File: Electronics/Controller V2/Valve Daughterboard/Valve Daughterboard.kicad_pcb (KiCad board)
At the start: 2 copper layers, 62 x 69.5 mm, 25 parts, among them J1 Conn_01x08, J10 Conn_01x10, J11 Conn_01x02, J12 Conn_01x02, J13 Conn_01x02, J14 Conn_01x02, J15 Conn_01x02, J16 Conn_01x02, J17 Conn_01x02, J18 Conn_01x02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

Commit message: Completed daughterboards.
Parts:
- H1, H2, H3, H4: footprint MountingHole:MountingHole_3.2mm_M3 -> MountingHole:MountingHole_6.4mm_M6
- moved J10 24.0 mm to (98.7, 92.1), turned to -90 degrees
- moved J20 23.3 mm to (91.5, 92.1), turned to -90 degrees
- moved J1 14.7 mm to (146.4, 70.2), turned to -90 degrees
- moved J19 13.8 mm to (140.6, 70.2), turned to -90 degrees
- moved H3 4.24 mm to (88.5, 124.5)
- moved H4 3.91 mm to (143.0, 124.5)
- moved H1 3.00 mm to (88.5, 60.0)
- moved H2 2.50 mm to (143.0, 60.0)
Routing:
- net /VALVE_E_MB: track 0.00 -> 129.7 mm
- net /VALVE_E_MA: track 0.00 -> 115.4 mm
- net /VALVE_D_MB: track 0.00 -> 101.2 mm
- net /VALVE_D_MA: track 0.00 -> 87.0 mm
- net /VALVE_C_MB: track 0.00 -> 72.8 mm
- net Net-(J11-Pin_1): track 0.00 -> 68.4 mm
- net +12V: track 0.00 -> 66.3 mm
- net Net-(J12-Pin_1): track 0.00 -> 61.8 mm
- net /VALVE_C_MA: track 0.00 -> 58.5 mm
- net /VALVE_B_DIR: track 0.00 -> 54.2 mm
- net Net-(J3-Pin_2): track 0.00 -> 49.7 mm
- net /VALVE_B_PWM: track 0.00 -> 48.1 mm
- net Net-(J2-Pin_2): track 0.00 -> 47.9 mm
- net /VALVE_B_MB: track 0.00 -> 45.5 mm
- net /VALVE_C_DIR: track 0.00 -> 42.1 mm
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- added copper zone on B.Cu, net GND
- added copper zone on F.Cu, net GND
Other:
- board size 62 x 69.5 mm -> 68.5 x 78.5 mm

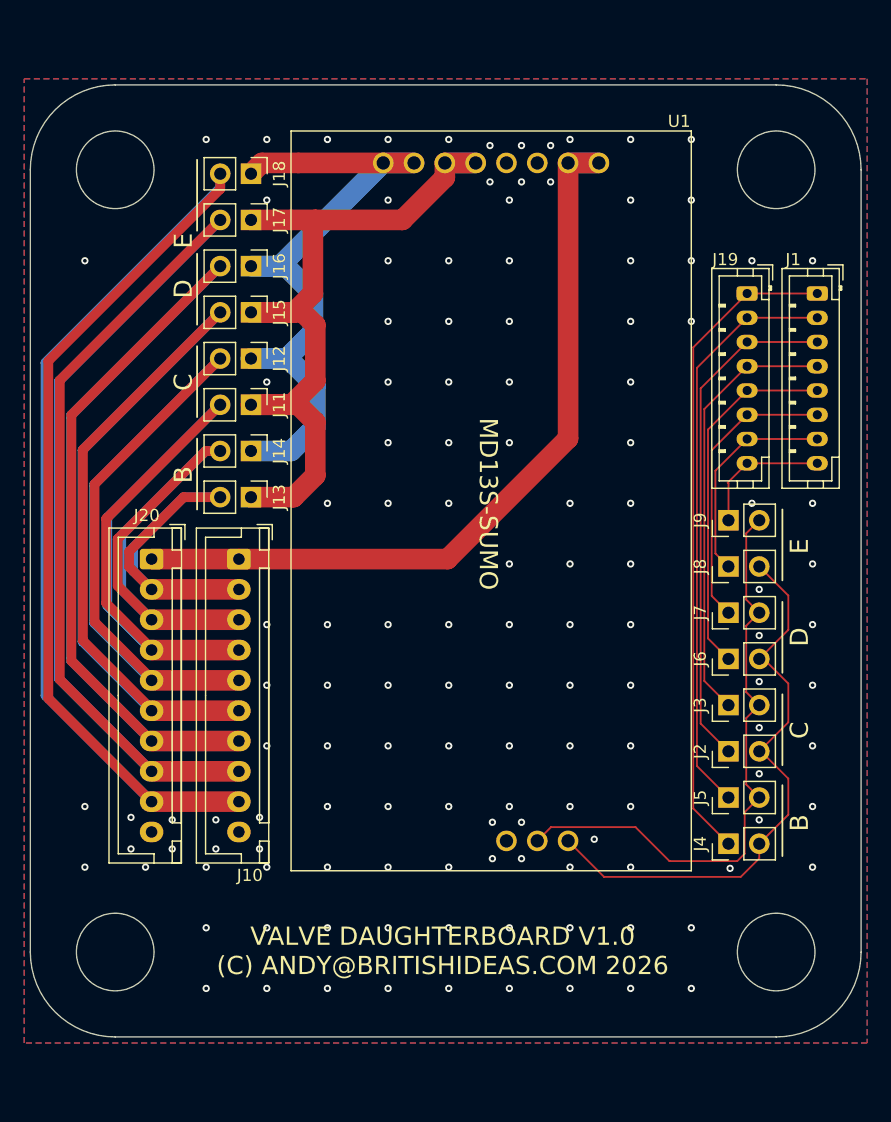
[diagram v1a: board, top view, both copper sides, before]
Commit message: Added relay to control output of valve E.
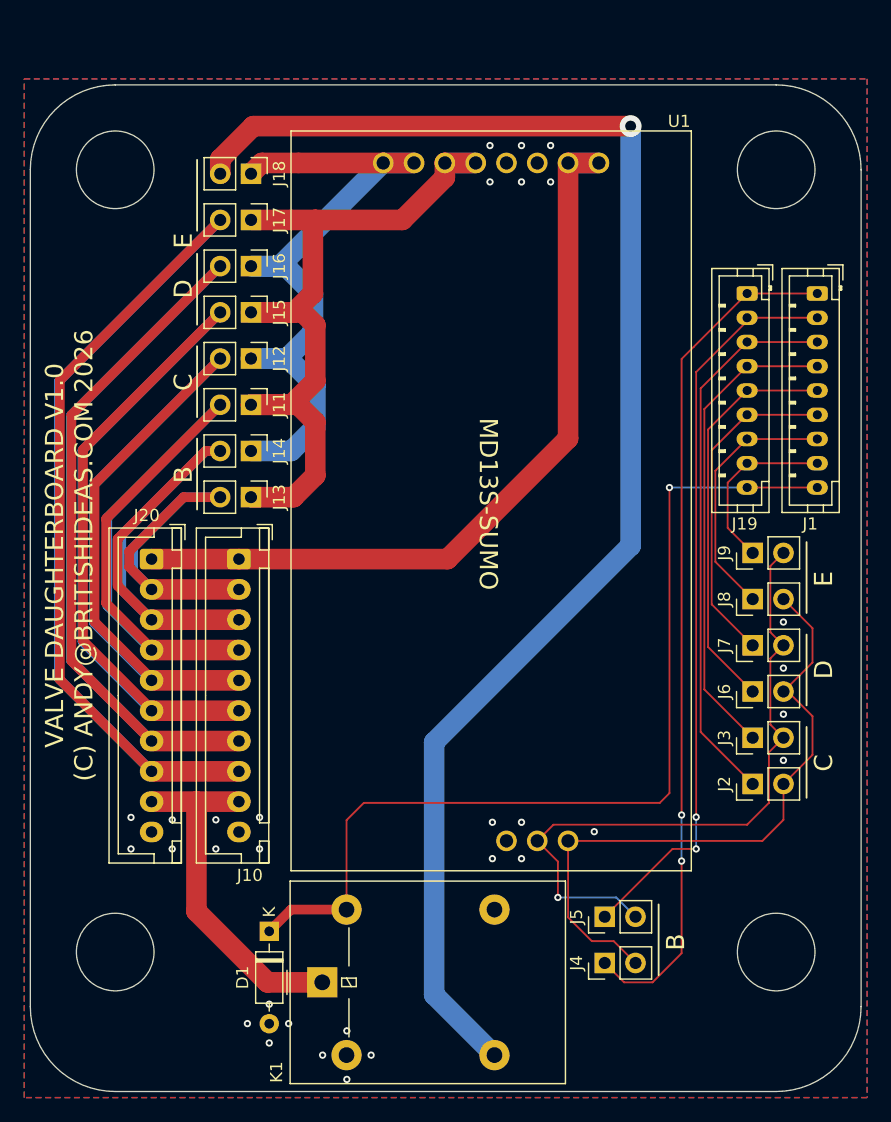
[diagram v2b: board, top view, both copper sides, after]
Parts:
- added D1: 1N4148, Diode_THT:D_DO-35_SOD27_P7.62mm_Horizontal, F.Cu at (101.2, 122.8)
- added K1: G5LE-1, Relay_THT:Relay_SPDT_Omron-G5LE-1, F.Cu at (105.6, 127.0)
- J1, J19: footprint Connector_JST:JST_PH_B8B-PH-K_1x08_P2.00mm_Vertical -> Connector_JST:JST_PH_B9B-PH-K_1x09_P2.00mm_Vertical
- moved J4 14.2 mm to (128.9, 125.4)
- moved J5 14.2 mm to (128.9, 121.6)
- moved J8 3.35 mm to (141.1, 95.4)
- moved J2 3.35 mm to (141.1, 110.6)
- moved J3 3.35 mm to (141.1, 106.8)
- moved J6 3.35 mm to (141.1, 103.0)
- moved J7 3.35 mm to (141.1, 99.2)
- moved J9 3.35 mm to (141.1, 91.6)
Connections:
- J18 pad 2: /VALVE_E_MB -> Net-(J18-Pin_2)
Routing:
- net Net-(J18-Pin_2): track 0.00 -> 121.5 mm, vias 0 -> 1
- net /VALVE_E_MB: track 129.7 -> 29.0 mm
- net /VALVE_E_EN: track 0.00 -> 79.4 mm, vias 0 -> 1
- net /VALVE_B_DIR: track 54.2 -> 70.4 mm, vias 0 -> 2
- net /VALVE_B_PWM: track 48.1 -> 61.2 mm, vias 0 -> 2
- net Net-(J2-Pin_2): track 47.9 -> 54.4 mm
- net Net-(J3-Pin_2): track 49.7 -> 55.7 mm, vias 0 -> 1
- net /VALVE_E_DIR: track 17.8 -> 21.3 mm
- net /VALVE_D_PWM: track 23.9 -> 27.4 mm
- net /VALVE_C_DIR: track 42.1 -> 45.6 mm
- net /VALVE_E_PWM: track 11.2 -> 14.7 mm
- net /VALVE_D_DIR: track 30.0 -> 33.5 mm
- net /VALVE_C_PWM: track 36.0 -> 39.5 mm
- net GND: vias 132 -> 31
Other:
- board size 68.5 x 78.5 mm -> 68.5 x 83 mm

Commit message: Working on autosteer support for V2 controller.
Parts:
- added J21: Conn_01x02, Connector_PinHeader_2.54mm:PinHeader_1x02_P2.54mm_Vertical, F.Cu at (111.2, 124.5)
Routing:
- net /VALVE_E_MB: track 29.0 -> 34.7 mm
- net Net-(J18-Pin_2): track 121.5 -> 125.2 mm
- net GND: vias 31 -> 118

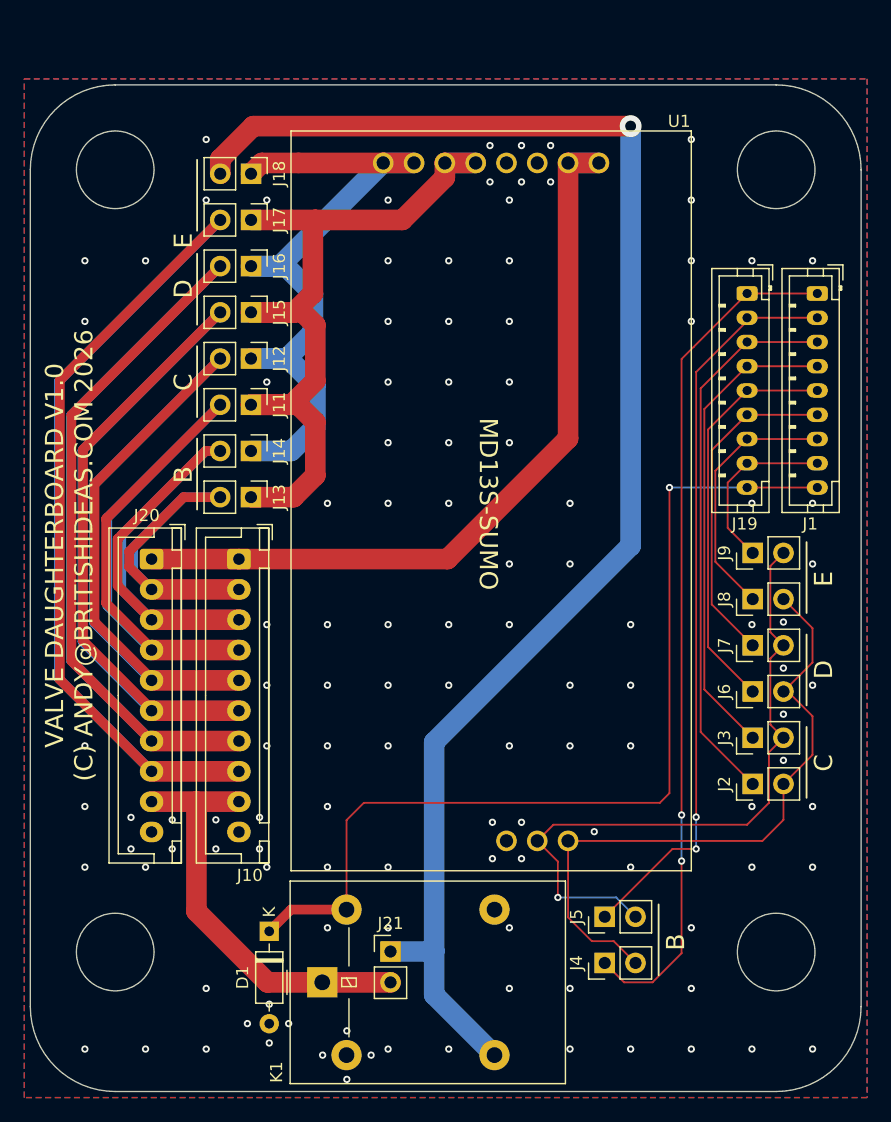
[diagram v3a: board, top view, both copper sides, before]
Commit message: Added connector to valve daugherboard for optional 12V to 24V converter.
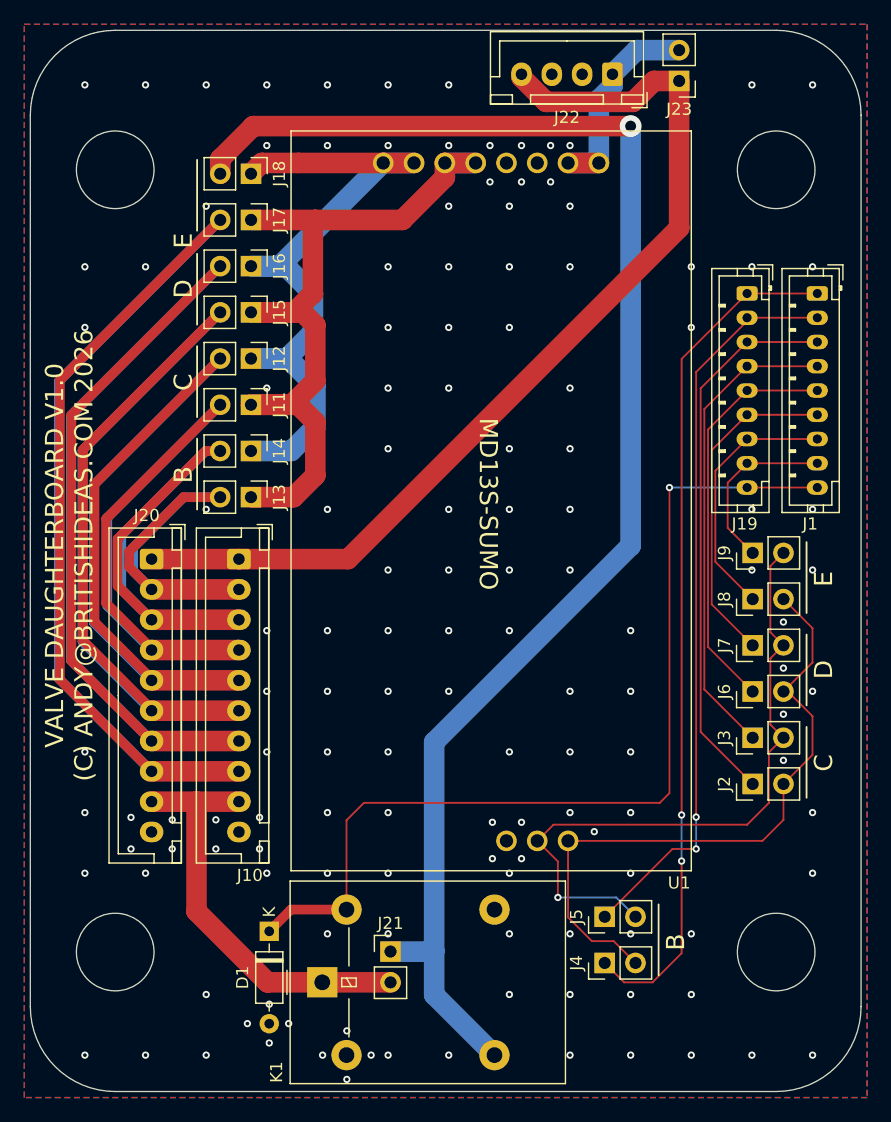
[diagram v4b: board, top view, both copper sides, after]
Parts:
- added J22: Conn_01x04, Connector_JST:JST_XH_B4B-XH-A_1x04_P2.50mm_Vertical, F.Cu at (129.5, 52.1)
- added J23: Conn_01x02, Connector_PinHeader_2.54mm:PinHeader_1x02_P2.54mm_Vertical, F.Cu at (135.0, 52.7)
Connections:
- U1 pad 4: +12V -> VDD
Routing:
- net VDD: track 0.00 -> 19.2 mm
- net +12V: track 66.3 -> 81.7 mm
- net GND: vias 118 -> 138
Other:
- board size 68.5 x 83 mm -> 68.5 x 87.5 mm
